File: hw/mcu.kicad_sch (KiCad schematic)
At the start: 23 parts, among them J301 SWD/JTAG, Q301 2N7002BK, U301 S32K148_144LQFP, U302 TPS3850G33

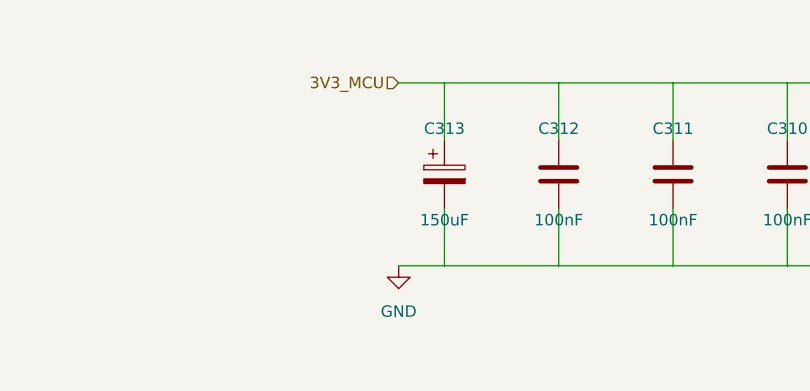
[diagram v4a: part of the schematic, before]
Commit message: Choose the three non-ceramic capacitors; the boost tank becomes a 2-can stack
C313: KEMET T599 150 uF polymer tantalum plus a 22 mOhm series resistor
(R306). No datasheet gives an ESR minimum, so the resistor is PDN-BULK's
floor; the pair is 21.8-72.2 mOhm and mcu_pdn passes both ends at 96 uF.

C211: Chemi-Con HXC 47 uF 63 V hybrid polymer. sensor_rail now runs its
worst corners at 26.3 uF (tolerance plus end of life) and passes.

C401 + C420: two HXC 82 uF 80 V in series, the owner's choice over one
160 V wet can, because no part rated above 100 V publishes a cold ESR.
Worst stack ESR 224 mOhm aged at -55 C; 18 A in 45 us at -40 C. The sims
run 41 uF, every check uses the 85.1 V worst low point, and the 22k bleed
is split 2 x 11k to balance the cans. Decisions log section 9.
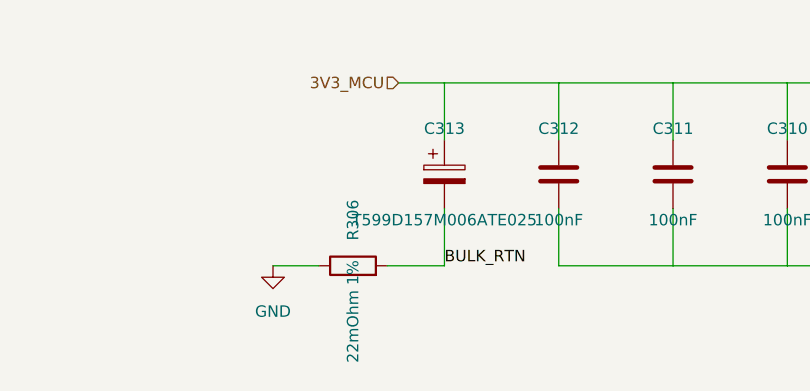
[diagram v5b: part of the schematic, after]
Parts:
- added R306: 22mOhm 1%, Resistor_SMD:R_1206_3216Metric, symbol Device:R
- C313: value 150uF -> T599D157M006ATE025; footprint (none) -> Capacitor_Tantalum_SMD:CP_EIA-7343-31_Kemet-D; Chosen (none) -> KEMET T599 polymer tantalum, 150 uF, 6.3 V (5.4 V at 125 C)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; Class (none) -> 150uF; ESR 20-50 mOhm over temperature -> pair 21.8-72.2 mOhm, -40/+125 C, end of life; MPN (none) -> T599D157M006ATE025; Note POLYMER, specified by an ESR BAND of 20-50 mOhm across -40/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 -> POLYMER tantalum, 25 mOhm max, IN SERIES with the 22 mOhm r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
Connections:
- net GND: now also R306.1; no longer C313.2
- new net BULK_RTN: C313.2, R306.2
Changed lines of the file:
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@@
       (effects (font (size 1.27 1.27)))
     )
-    (property "Value" "150uF" (id 1) (at 273.0 400.08 0)
+    (property "Value" "T599D157M006ATE025" (id 1) (at 273.0 400.08 0)
       (effects (font (size 1.27 1.27)))
     )
-    (property "Footprint" "" (id 2) (at 273.0 395 0)
+    (property "Footprint" "Capacitor_Tantalum_SMD:CP_EIA-7343-31_Kemet-D" (id 2) (at 273.0 395 0)
       (effects (font (size 1.27 1.27)) hide)
     )
@@
       (effects (font (size 1.27 1.27)) hide)
     )
-    (property "Source" "mcu_pdn.cir bulk; bom_requirements PDN-BULK" (id 4) (at 273.0 395 0)
+    (property "MPN" "T599D157M006ATE025" (id 4) (at 273.0 395 0)
       (effects (font (size 1.27 1.27)) hide)
     )
-    (property "Note" "POLYMER, specified by an ESR BAND of 20-50 mOhm across -40/+125 C. Not a ceiling: at 20 mOhm the PDN peak climbs back to 92 mOhm, because this part's ESR is also the damping." (id 5) (at 273.0 395 0)
+    (property "Class" "150uF" (id 5) (at 273.0 395 0)
       (effects (font (size 1.27 1.27)) hide)
     )
-    (property "ESR" "20-50 mOhm over temperature" (id 6) (at 273.0 395 0)
+    (property "Chosen" "KEMET T599 polymer tantalum, 150 uF, 6.3 V (5.4 V at 125 C), 25 mOhm max at 100 kHz, -55/+150 C, AEC-Q200. In series with a 22 mOhm resistor: the pair is PDN-BULK's ESR band" (id 6) (at 273.0 395 0)
+      (effects (font (size 1.27 1.27)) hide)
+    )
+    (property "Source" "mcu_pdn.cir bulk; bom_requirements PDN-BULK" (id 7) (at 273.0 395 0)
+      (effects (font (size 1.27 1.27)) hide)
+    )
+    (property "Note" "POLYMER tantalum, 25 mOhm max, IN SERIES with the 22 mOhm resistor beside it. The pair is the ESR band: a capacitor datasheet gives a maximum, never a minimum, so the resistor is the floor (decisions log 9)." (id 8) (at 273.0 395 0)
+      (effects (font (size 1.27 1.27)) hide)
+    )
+    (property "ESR" "pair 21.8-72.2 mOhm, -40/+125 C, end of life" (id 9) (at 273.0 395 0)
       (effects (font (size 1.27 1.27)) hide)
     )
@@
     (stroke (width 0) (type default))
   )
-  (wire (pts (xy 273.0 405.16) (xy 285.7 405.16))
-    (stroke (width 0) (type default))
+  (label "BULK_RTN" (at 273.0 405.16 0)
+    (effects (font (size 1.27 1.27)) (justify left bottom))
   )
-  (symbol (lib_id "power:GND") (at 267.92 405.16 0) (unit 1)
+  (symbol (lib_id "Device:R") (at 262.84 405.16 90) (unit 1)
     (in_bom yes) (on_board yes) (fields_autoplaced)
-    (property "Reference" "#PWR309" (id 0) (at 267.92 400.08000000000004 0)
+    (property "Reference" "R306" (id 0) (at 262.84 400.08000000000004 0)
+      (effects (font (size 1.27 1.27)))
+    )
+    (property "Value" "22mOhm 1%" (id 1) (at 262.84 410.24 0)
+      (effects (font (size 1.27 1.27)))
+    )
+    (property "Footprint" "Resistor_SMD:R_1206_3216Metric" (id 2) (at 262.84 405.16 0)
       (effects (font (size 1.27 1.27)) hide)
     )
-    (property "Value" "GND" (id 1) (at 267.92 410.24 0)
-      (effects (font (size 1.27 1.27)))
-    )
-    (property "Footprint" "" (id 2) (at 267.92 405.16 0)
+    (property "Datasheet" "~" (id 3) (at 262.84 405.16 0)
       (effects (font (size 1.27 1.27)) hide)
     )
-    (property "Datasheet" "~" (id 3) (at 267.92 405.16 0)
+    (property "Source" "mcu_pdn.cir Rb; decisions log 9" (id 4) (at 262.84 405.16 0)
+      (effects (font (size 1.27 1.27)) hide)
+    )
+    (property "Note" "Damping for the regulator-against-bulk resonance that the polymer bulk is too good to provide. Below 17 mOhm total the PDN peak passes 100 mOhm." (id 5) (at 262.84 405.16 0)
       (effects (font (size 1.27 1.27)) hide)
     )
   )
-  (wire (pts (xy 267.92 405.16) (xy 273.0 405.16))
+  (wire (pts (xy 266.65 405.16) (xy 273.0 405.16))
     (stroke (width 0) (type default))
   )
+  (wire (pts (xy 259.03 405.16) (xy 253.95 405.16))
+    (stroke (width 0) (type default))
+  )
+  (symbol (lib_id "power:GND") (at 253.95 405.16 0) (unit 1)
+    (in_bom yes) (on_board yes) (fields_autoplaced)
+    (property "Reference" "#PWR309" (id 0) (at 253.94999999999996 400.08000000000004 0)
+      (effects (font (size 1.27 1.27)) hide)
+    )
+    (property "Value" "GND" (id 1) (at 253.94999999999996 410.24 0)
+      (effects (font (size 1.27 1.27)))
+    )
+    (property "Footprint" "" (id 2) (at 253.94999999999996 405.16 0)
+      (effects (font (size 1.27 1.27)) hide)
+    )
+    (property "Datasheet" "~" (id 3) (at 253.94999999999996 405.16 0)
+      (effects (font (size 1.27 1.27)) hide)
+    )
+  )
   (symbol (lib_id "Connector:Conn_ARM_JTAG_SWD_10") (at 385.0 330.0 0) (unit 1)

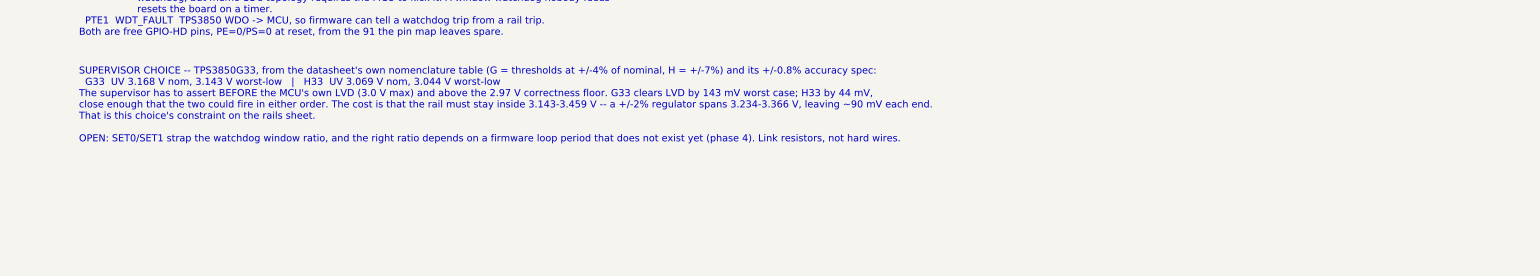
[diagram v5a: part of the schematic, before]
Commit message: Bible: record the firmware SIL decisions
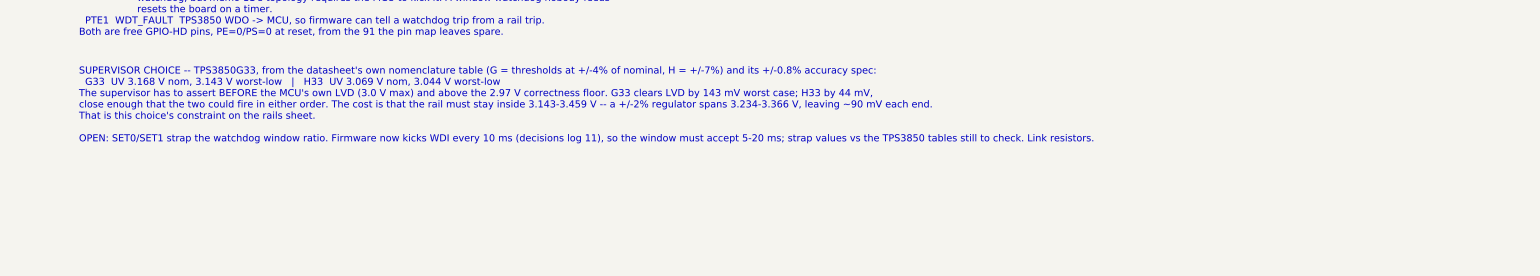
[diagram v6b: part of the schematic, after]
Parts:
- R303: Source TPS3850 sec.6.6 -- window ratio strap. OPEN: the ratio depends on a firmware loop period that does not exist yet, phase 4 -> TPS3850 sec.6.6 -- window ratio strap. OPEN: the ratio depends on the firmware kick period: 10 ms, window 5-20 ms (decisions log 11)
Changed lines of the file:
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@@
       (effects (font (size 1.27 1.27)) hide)
     )
-    (property "Source" "TPS3850 sec.6.6 -- window ratio strap. OPEN: the ratio depends on a firmware loop period that does not exist yet, phase 4" (id 4) (at 51.42 375.48 0)
+    (property "Source" "TPS3850 sec.6.6 -- window ratio strap. OPEN: the ratio depends on the firmware kick period: 10 ms, window 5-20 ms (decisions log 11)" (id 4) (at 51.42 375.48 0)
       (effects (font (size 1.27 1.27)) hide)
     )
@@
     (effects (font (size 1.6 1.6)) (justify left))
   )
-  (text "SUPERVISOR CHOICE -- TPS3850G33, from the datasheet's own nomenclature table (G = thresholds at +/-4% of nominal, H = +/-7%) and its +/-0.8% accuracy spec:\n  G33  UV 3.168 V nom, 3.143 V worst-low   |   H33  UV 3.069 V nom, 3.044 V worst-low\nThe supervisor has to assert BEFORE the MCU's own LVD (3.0 V max) and above the 2.97 V correctness floor. G33 clears LVD by 143 mV worst case; H33 by 44 mV,\nclose enough that the two could fire in either order. The cost is that the rail must stay inside 3.143-3.459 V -- a +/-2% regulator spans 3.234-3.366 V, leaving ~90 mV each end.\nThat is this choice's constraint on the rails sheet.\n\nOPEN: SET0/SET1 strap the watchdog window ratio, and the right ratio depends on a firmware loop period that does not exist yet (phase 4). Link resistors, not hard wires." (at 40.0 155.0 0)
+  (text "SUPERVISOR CHOICE -- TPS3850G33, from the datasheet's own nomenclature table (G = thresholds at +/-4% of nominal, H = +/-7%) and its +/-0.8% accuracy spec:\n  G33  UV 3.168 V nom, 3.143 V worst-low   |   H33  UV 3.069 V nom, 3.044 V worst-low\nThe supervisor has to assert BEFORE the MCU's own LVD (3.0 V max) and above the 2.97 V correctness floor. G33 clears LVD by 143 mV worst case; H33 by 44 mV,\nclose enough that the two could fire in either order. The cost is that the rail must stay inside 3.143-3.459 V -- a +/-2% regulator spans 3.234-3.366 V, leaving ~90 mV each end.\nThat is this choice's constraint on the rails sheet.\n\nOPEN: SET0/SET1 strap the watchdog window ratio. Firmware now kicks WDI every 10 ms (decisions log 11), so the window must accept 5-20 ms; strap values vs the TPS3850 tables still to check. Link resistors." (at 40.0 155.0 0)
     (effects (font (size 1.6 1.6)) (justify left))
   )

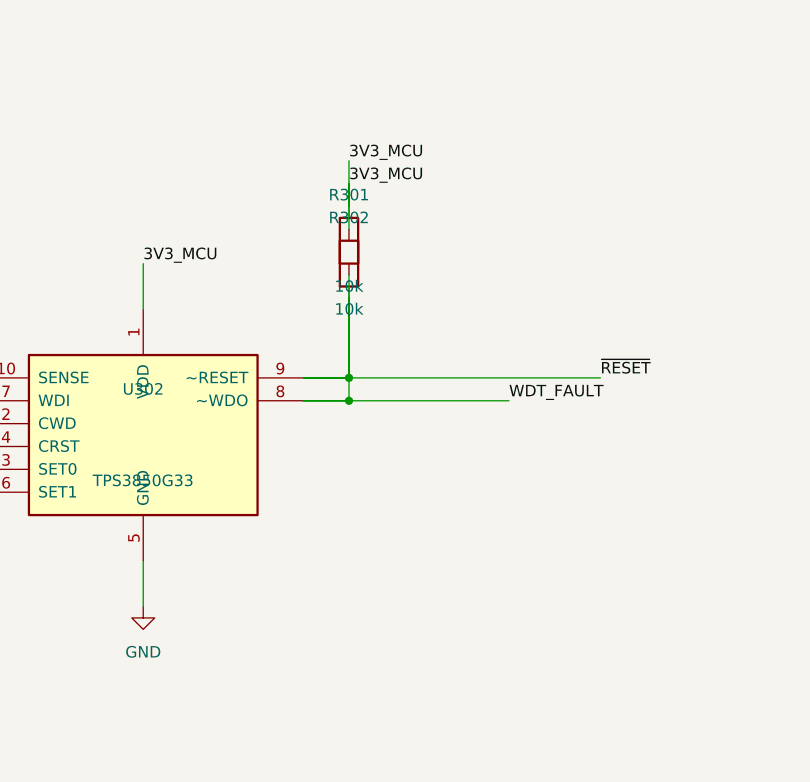
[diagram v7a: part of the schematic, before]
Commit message: Separate the supervisor's RESET and WDO nets: their pullups overlapped and shorted them
The two 10k pullups sat in one column 2.54 mm apart, and RESET's lead
wire ran through WDO's pullup pin. RESET, WDO, the MCU reset pin, the
kill inverter gate and WDT_FAULT were one net, so firmware could not
tell a watchdog trip from a rail trip. WDO's pullup now hangs below its
pin. check_netlist gains MUST_SEPARATE so it cannot come back; the
production board's seven pads were moved onto the new net in place.
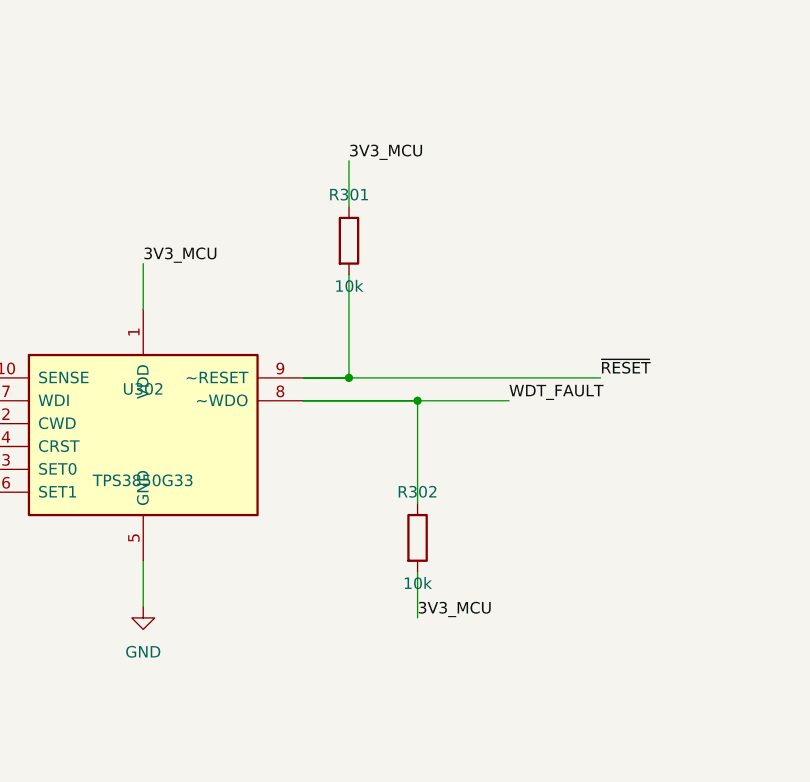
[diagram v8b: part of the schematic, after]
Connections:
- net 3V3_MCU: now also R302.2; no longer R302.1
- net WDT_FAULT: now also R302.1; no longer J301.10 (~{RESET}), Q301.1 (G), R301.2, R302.2, U301.141 (PTA5[PU]), U302.9 (~RESET)
- new net ~{RESET}: J301.10 (~{RESET}), Q301.1 (G), R301.2, U301.141 (PTA5[PU]), U302.9 (~RESET)
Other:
- moved on the sheet: R302
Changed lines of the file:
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@@
   (junction (at 142.86 338.65) (diameter 0) (color 0 0 0 0)
   )
-  (symbol (lib_id "Device:R") (at 142.86 325.95 0) (unit 1)
+  (symbol (lib_id "Device:R") (at 150.48 356.43 0) (unit 1)
     (in_bom yes) (on_board yes) (fields_autoplaced)
-    (property "Reference" "R302" (id 0) (at 142.86 320.87 0)
+    (property "Reference" "R302" (id 0) (at 150.48 351.35 0)
       (effects (font (size 1.27 1.27)))
     )
-    (property "Value" "10k" (id 1) (at 142.86 331.03 0)
+    (property "Value" "10k" (id 1) (at 150.48 361.51 0)
       (effects (font (size 1.27 1.27)))
     )
-    (property "Footprint" "Resistor_SMD:R_0603_1608Metric" (id 2) (at 142.86 325.95 0)
+    (property "Footprint" "Resistor_SMD:R_0603_1608Metric" (id 2) (at 150.48 356.43 0)
       (effects (font (size 1.27 1.27)) hide)
     )
-    (property "Datasheet" "~" (id 3) (at 142.86 325.95 0)
+    (property "Datasheet" "~" (id 3) (at 150.48 356.43 0)
       (effects (font (size 1.27 1.27)) hide)
     )
-    (property "Source" "TPS3850 datasheet sec.5 -- open-drain output pullup, 1k-100k to VDD" (id 4) (at 142.86 325.95 0)
+    (property "Source" "TPS3850 datasheet sec.5 -- open-drain output pullup, 1k-100k to VDD" (id 4) (at 150.48 356.43 0)
       (effects (font (size 1.27 1.27)) hide)
     )
   )
-  (wire (pts (xy 142.86 322.14) (xy 142.86 317.06))
+  (wire (pts (xy 150.48 360.24) (xy 150.48 365.32))
     (stroke (width 0) (type default))
   )
-  (label "3V3_MCU" (at 142.86 317.06 0)
+  (label "3V3_MCU" (at 150.48 365.32 0)
     (effects (font (size 1.27 1.27)) (justify left bottom))
   )
-  (wire (pts (xy 142.86 329.76) (xy 142.86 341.19))
+  (wire (pts (xy 150.48 352.62) (xy 150.48 341.19))
     (stroke (width 0) (type default))
   )
-  (wire (pts (xy 137.78 341.19) (xy 142.86 341.19))
+  (wire (pts (xy 137.78 341.19) (xy 150.48 341.19))
     (stroke (width 0) (type default))
   )
-  (junction (at 142.86 341.19) (diameter 0) (color 0 0 0 0)
+  (junction (at 150.48 341.19) (diameter 0) (color 0 0 0 0)
   )
   (wire (pts (xy 137.78 338.65) (xy 170.8 338.65))
